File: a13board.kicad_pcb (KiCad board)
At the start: 4 copper layers, 122.3 x 91.1 mm, 147 parts, among them U1 H27UBG8T2A/TSOP48, U2 A13, U3 H5TQ2G43CFR, U4 H5TQ2G43CFR, U5 OLIMEX_IC_AXP209, U6 SY8008BAAC, U7 SY8008BAAC

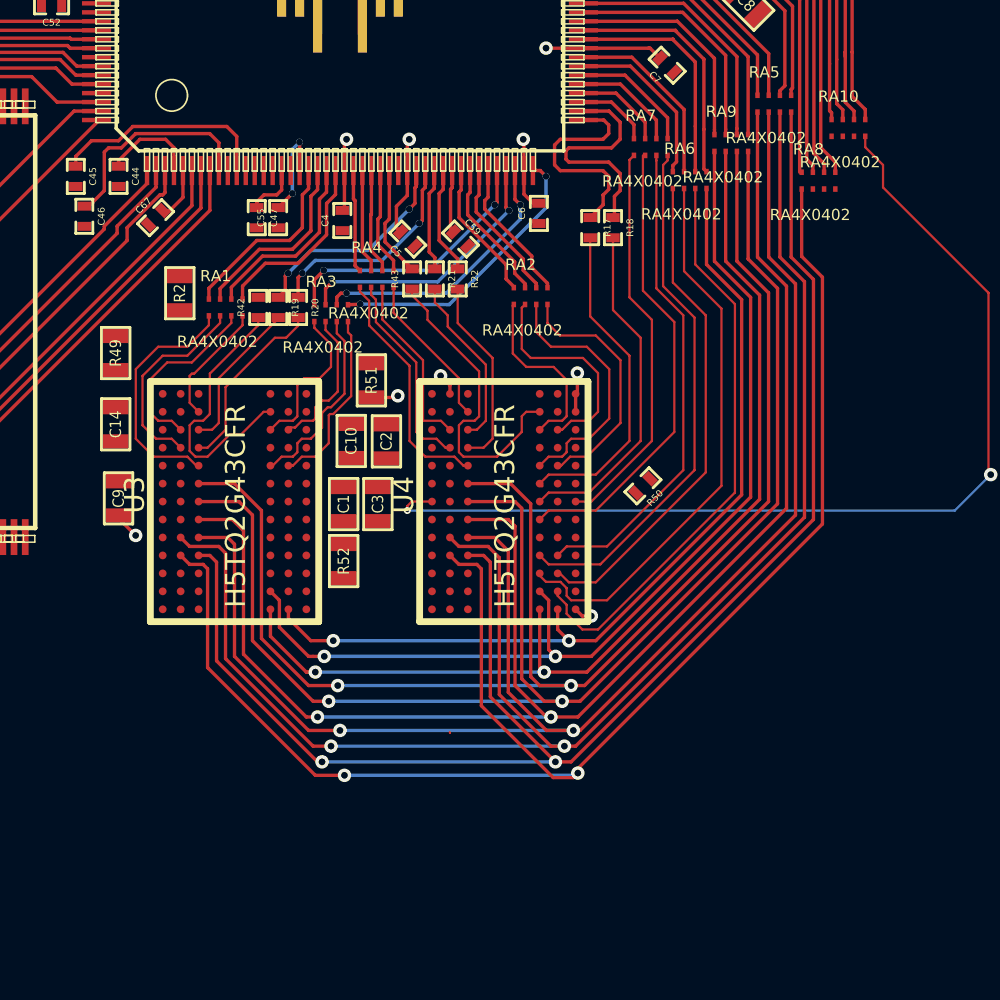
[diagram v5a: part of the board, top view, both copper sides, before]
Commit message: Routed ground poly and most of ddr3
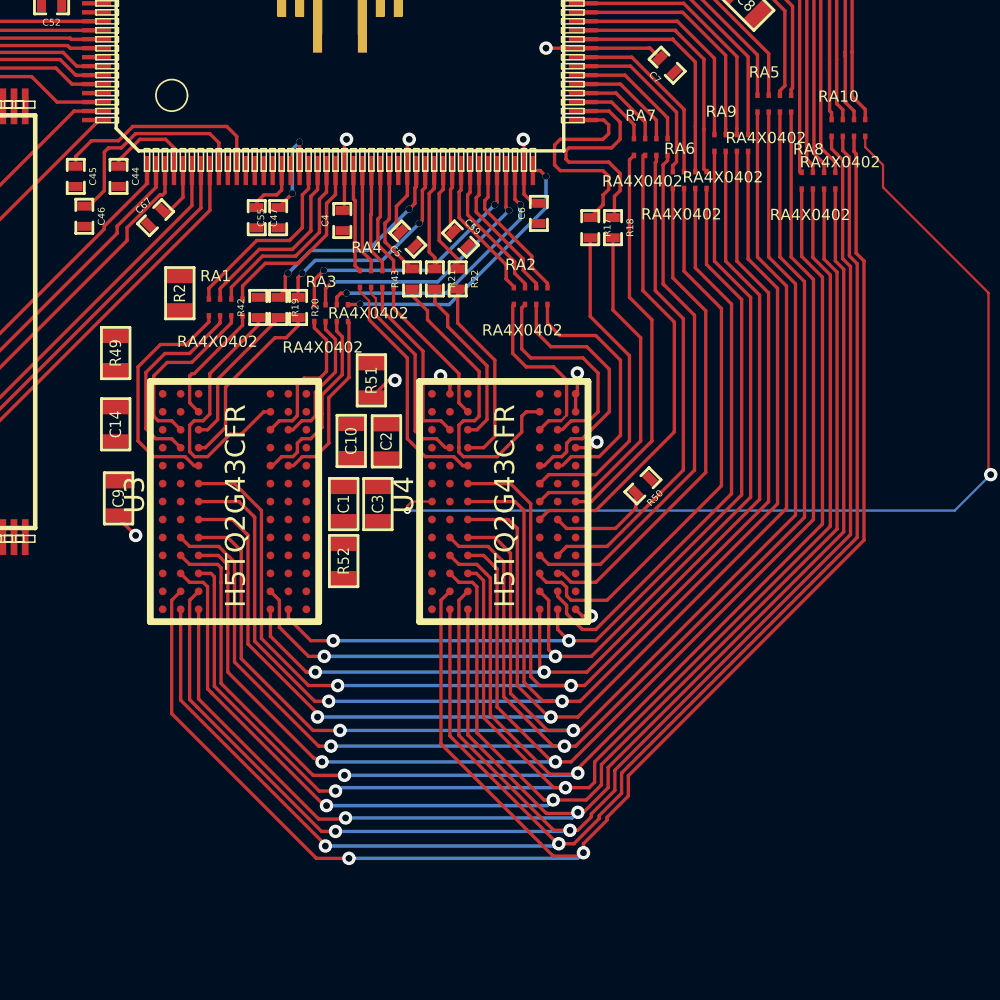
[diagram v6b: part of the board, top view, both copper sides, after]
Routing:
- net /DRAM/DDR3_A7: track 0.00 -> 79.5 mm, vias 0 -> 2
- net /DRAM/DDR3_A9: track 0.00 -> 74.3 mm, vias 0 -> 2
- net /DRAM/DDR3_RST: track 0.14 -> 74.0 mm, vias 0 -> 2
- net /DRAM/DDR3_A5: track 0.00 -> 69.8 mm, vias 0 -> 2
- net /DRAM/DDR3_A13: track 0.00 -> 68.2 mm, vias 0 -> 2
- net /DRAM/DDR3_A2: track 0.00 -> 67.7 mm, vias 0 -> 2
- net N-0000022: track 0.00 -> 4.70 mm
- net GND: track 0.82 -> 1.88 mm, vias 1 -> 2
- added copper zone on Inner2.Cu, net GND

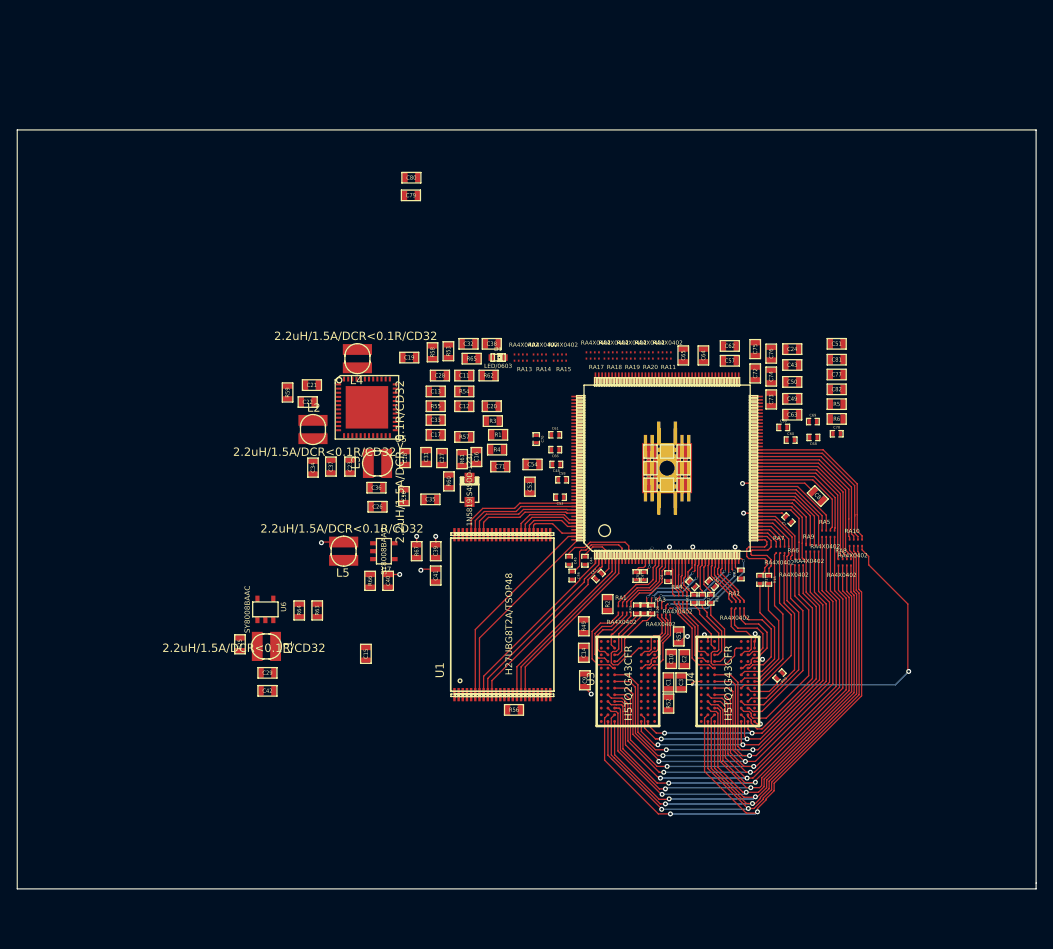
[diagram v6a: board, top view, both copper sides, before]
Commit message: more routing of DDR3
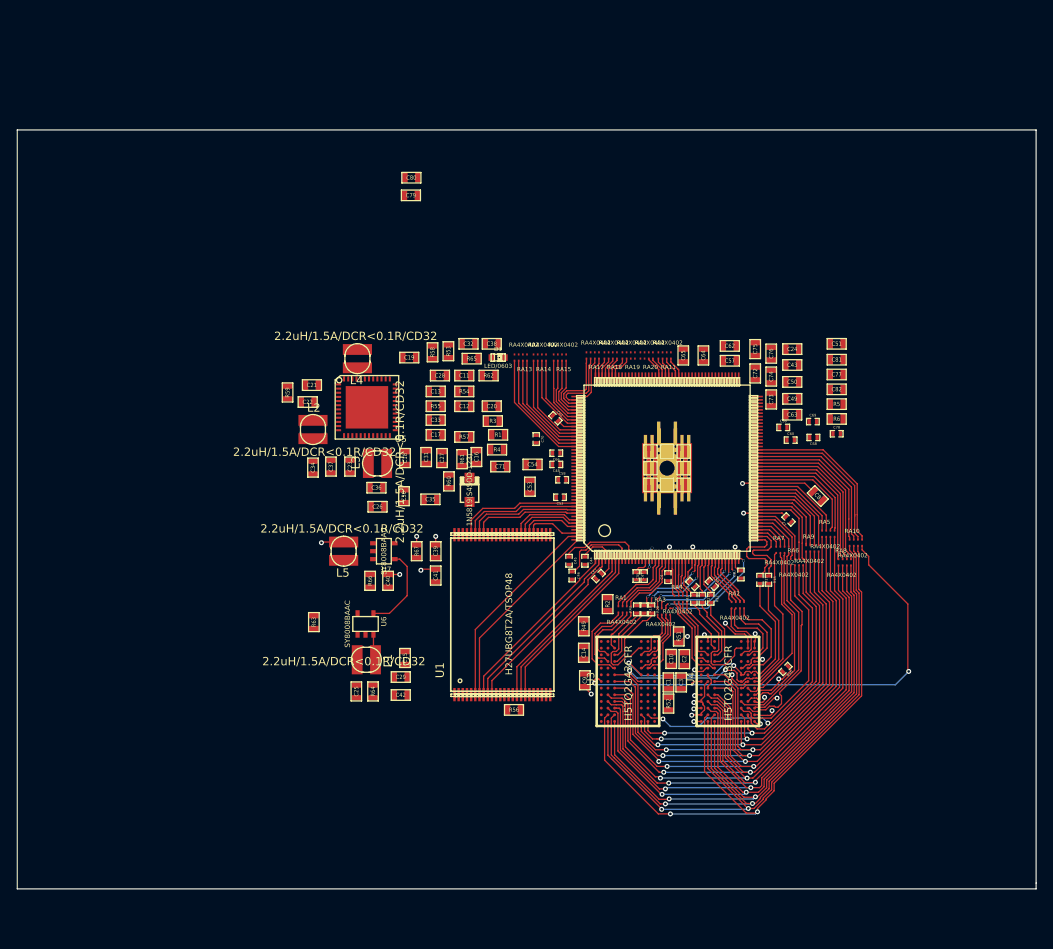
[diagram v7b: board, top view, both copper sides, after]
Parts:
- moved C29 16.0 mm to (81.5, 116.1)
- moved C42 16.0 mm to (81.5, 118.2)
- moved C25 15.1 mm to (76.2, 117.8)
- moved R64 13.2 mm to (78.2, 117.8)
- moved U6 12.1 mm to (77.3, 109.7)
- moved L1 12.1 mm to (77.4, 114.0)
- moved C15 4.73 mm to (82.0, 113.8)
- moved C61 2.00 mm to (100.1, 85.0), turned to 135 degrees
- moved R63 1.46 mm to (71.1, 109.5)
- moved R50 1.06 mm to (127.7, 115.1)
- moved C66 0.44 mm to (100.2, 89.2)
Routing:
- net GND: track 1.88 -> 21.4 mm, vias 2 -> 8
- net /DRAM/DDR3_CK: track 14.8 -> 32.6 mm, vias 0 -> 2
- net /DRAM/DDR3_CK_N: track 15.2 -> 32.7 mm, vias 0 -> 2
- net /DRAM/DDR3_A6: track 25.6 -> 41.6 mm, vias 0 -> 2
- net VMEM: track 75.7 -> 91.5 mm, vias 14 -> 20
- net N-00000303: track 0.00 -> 14.7 mm
- net N-00000289: track 0.00 -> 14.0 mm
- net N-00000291: track 0.00 -> 13.4 mm
- net /DRAM/DDR3_ODT: track 45.4 -> 58.7 mm, vias 2 -> 3
- net N-00000293: track 0.00 -> 12.8 mm
- net N-00000295: track 0.00 -> 12.1 mm
- net N-00000306: track 0.00 -> 11.4 mm
- net RESET_SW: track 0.00 -> 10.3 mm
- net N-00000311: track 0.00 -> 9.89 mm
- net N-00000314: track 0.00 -> 9.27 mm
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
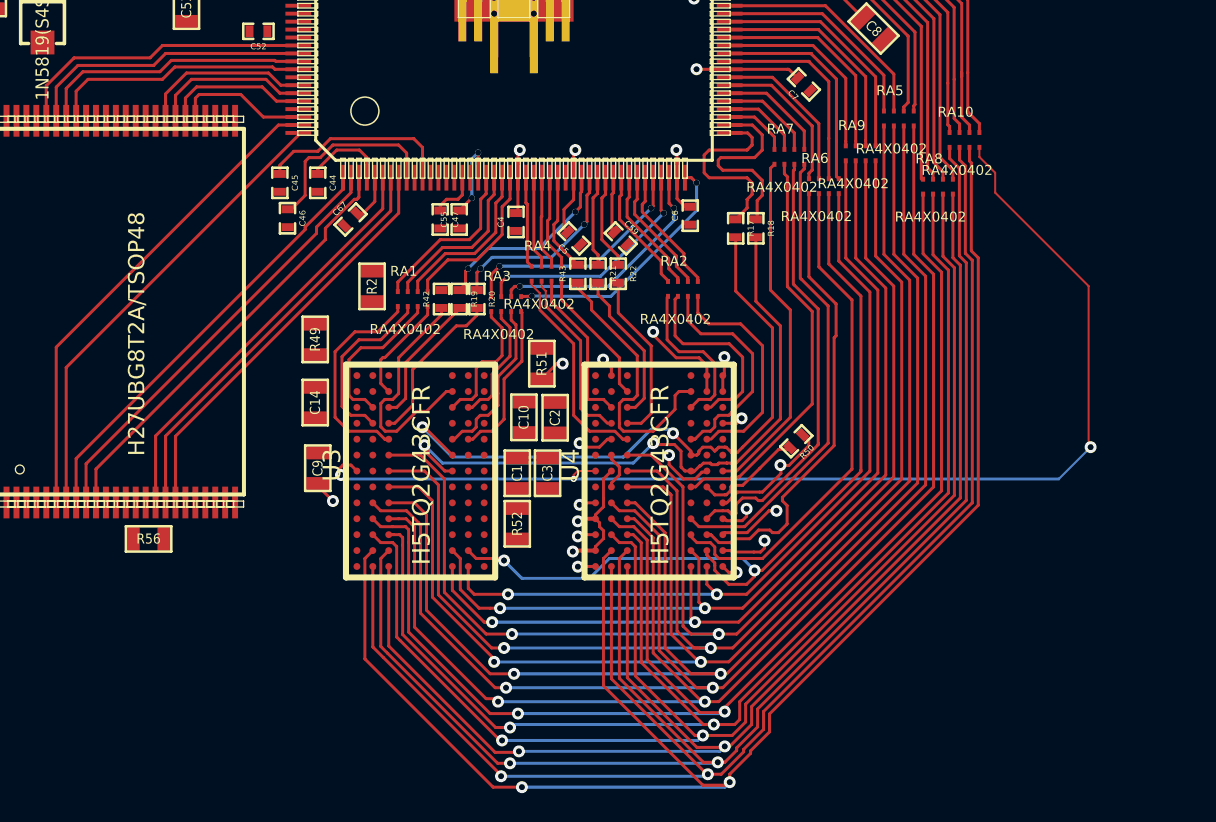
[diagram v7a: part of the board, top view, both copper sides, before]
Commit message: more routing of ddr3, found smaller approach, bga-escaping VMEM and GND
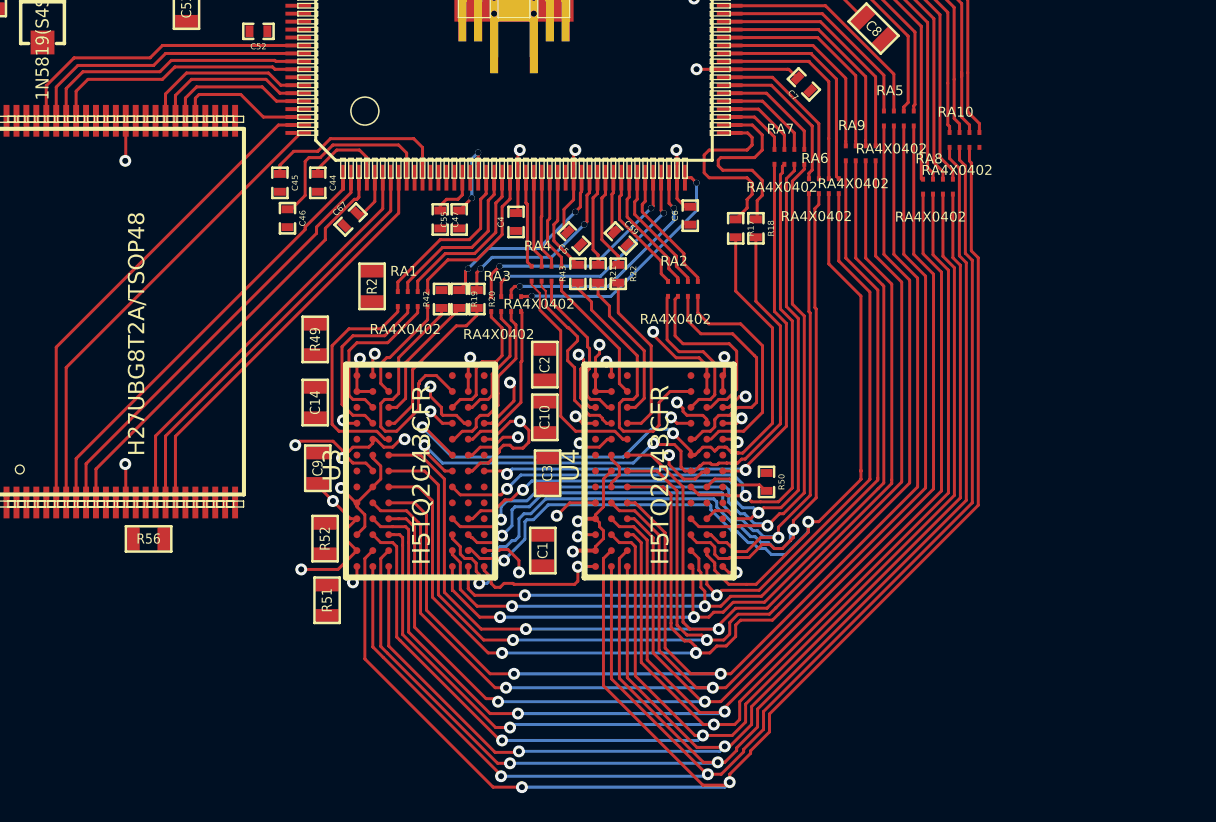
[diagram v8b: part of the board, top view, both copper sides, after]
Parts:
- moved R51 16.1 mm to (104.1, 123.1)
- moved R52 9.69 mm to (104.0, 120.0), turned to 270 degrees
- moved C1 4.09 mm to (115.0, 120.6)
- moved C2 2.72 mm to (115.0, 111.2)
- moved R50 2.54 mm to (126.2, 117.2), turned to 90 degrees
- moved C10 1.05 mm to (115.0, 113.9)
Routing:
- net /DRAM/DDR3_ODT: track 58.7 -> 0.00 mm, vias 3 -> 0
- net GND: track 21.4 -> 52.3 mm, vias 8 -> 20
- net VMEM: track 91.5 -> 118.4 mm, vias 20 -> 28
- net /DRAM/DDR3_A1: track 25.3 -> 48.2 mm, vias 0 -> 2
- net /DRAM/DDR3_A12: track 23.5 -> 42.0 mm, vias 0 -> 2
- net /DRAM/DDR3_A10: track 20.5 -> 38.3 mm, vias 0 -> 2
- net /DRAM/DDR3_A4: track 23.3 -> 41.0 mm, vias 0 -> 2
- net /DRAM/DDR3_BA1: track 22.3 -> 38.8 mm, vias 0 -> 2
- net /DRAM/DDR3_CKE: track 17.7 -> 31.1 mm, vias 0 -> 2
- net /DRAM/DDR3_A6: track 41.6 -> 47.5 mm
- net N-0000022: track 5.44 -> 3.41 mm
- net /DRAM/DDR3_DM0: track 12.0 -> 13.5 mm
- net /DRAM/DDR3_D4: track 10.7 -> 11.4 mm
- net /DRAM/DDR3_D14: track 11.4 -> 12.0 mm
